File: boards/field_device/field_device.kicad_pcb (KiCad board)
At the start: 4 copper layers, 50 x 55 mm, 52 parts, among them SW1 TS-1088-AR02016, U1 CHT20MEMS, U2 STM32C051F8P6, U3 SPA06-003, U4 CN3163, U5 TPS63900, U6 SX1262IMLTRT, Y1 X322532MMB4SI

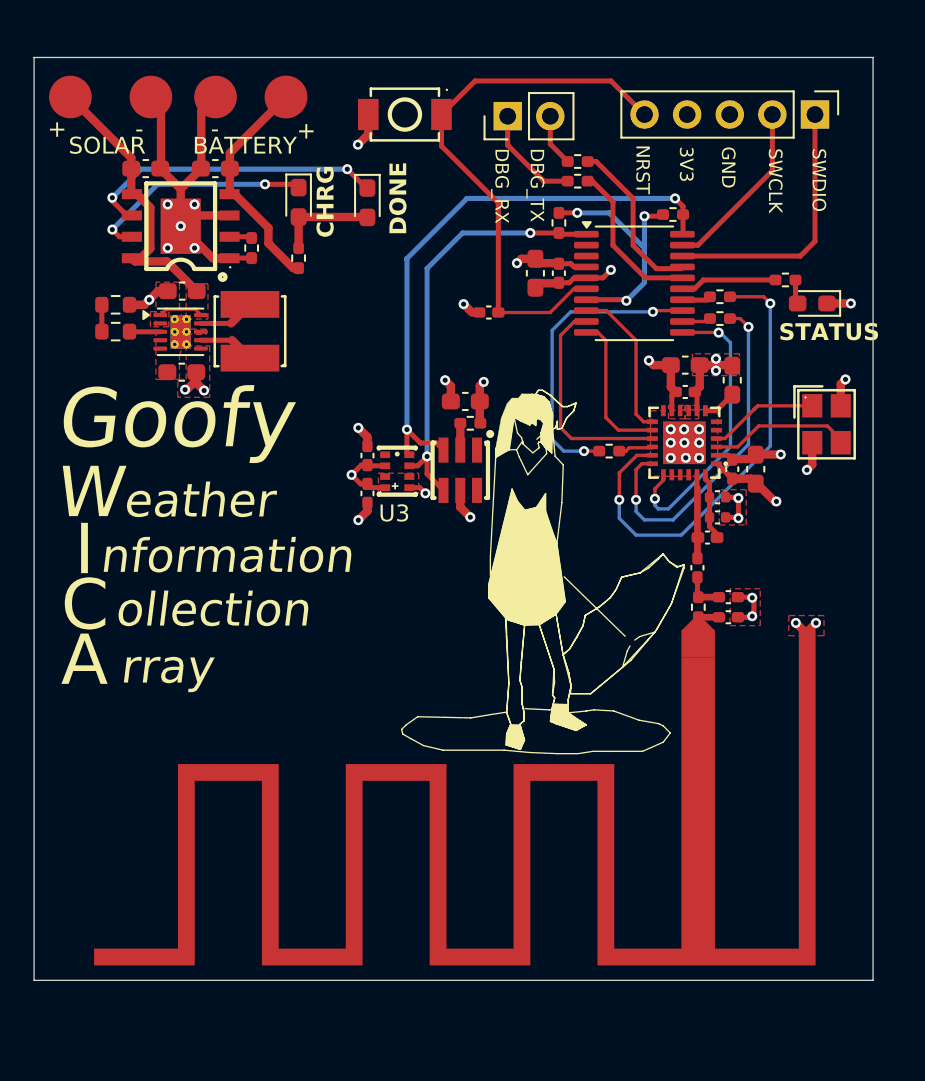
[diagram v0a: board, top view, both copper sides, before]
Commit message: change components to fit manufacturing capability
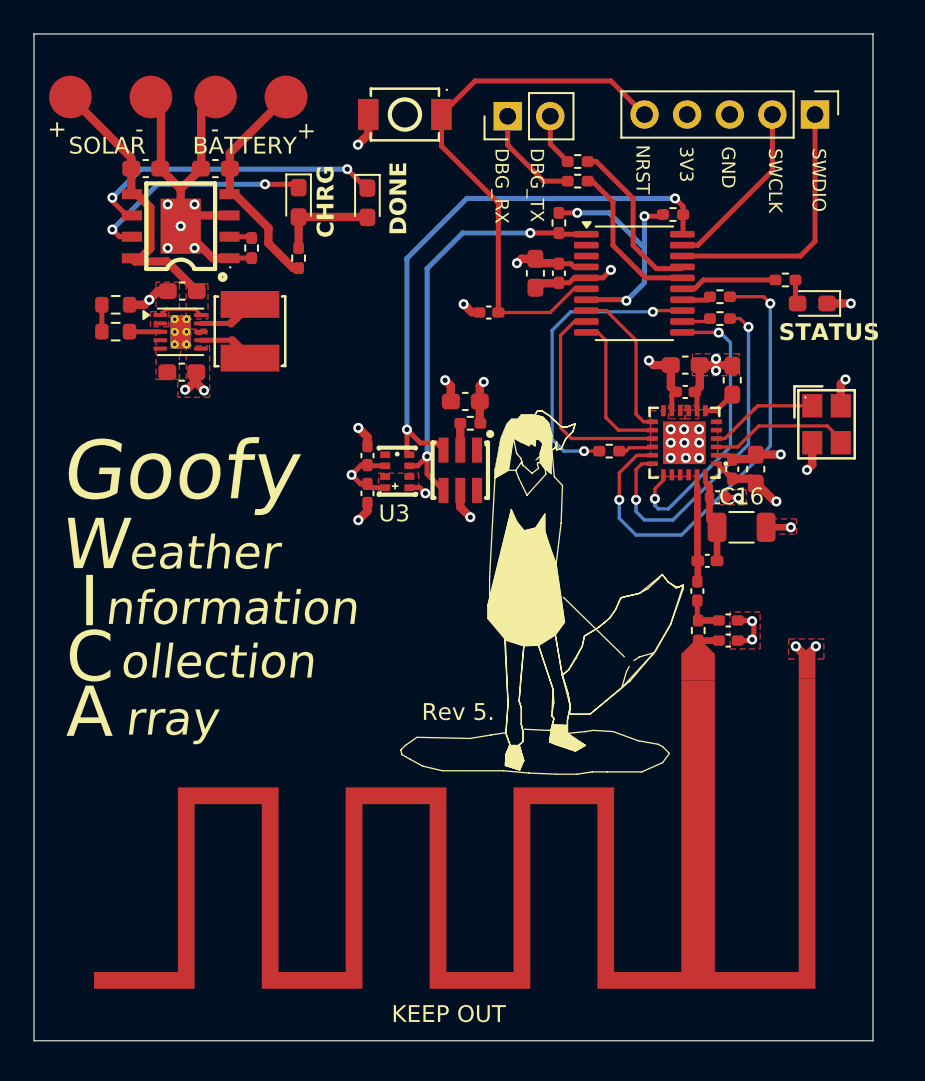
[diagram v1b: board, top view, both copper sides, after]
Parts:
- C1, C11, C12, C13: value 10u -> 10uF
- C14, C15, C2: value 100n -> 100nF
- C16: value 47n -> 47nF C0G; footprint Capacitor_SMD:C_0402_1005Metric -> Resistor_SMD:R_1206_3216Metric
- C17, C18: value 100p -> 100p C0G
- L2: value 47n -> 47nH
- moved C16 1.55 mm to (71.9, 51.4)
- moved AE1 1.39 mm to (76.3, 78.9)
- moved C18 1.39 mm to (69.2, 55.2)
- moved C19 1.39 mm to (71.1, 57.0)
- moved C20 1.39 mm to (71.1, 58.1)
- moved L2 1.39 mm to (69.8, 53.4)
- moved R15 1.39 mm to (69.3, 57.6)
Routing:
- net /lora_module/VR_PA: track 4.11 -> 6.20 mm
- net /lora_module/RFO: track 8.78 -> 10.0 mm
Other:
- board size 50 x 55 mm -> 50 x 60 mm
- board text added: "KEEP OUT"
- board text added: "Rev 5."

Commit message: idk atp
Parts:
- C1, C11, C12, C13, C3, C7, C8, C9: value 10uF -> CL10A106KP8NNNC 10uF
- C10: value 22uF -> CL10A226MQ8NRNC 22uF
- C14, C15, C2, C4, C5, C6: value 100nF -> CL05B104KO5NNNC 100nF
- C16: value 47nF C0G -> 47nF
- C17, C18: value 100p C0G -> 0402CG101J500NT 100pF
- L2: footprint Inductor_SMD:L_0402_1005Metric_Pad0.77x0.64mm_HandSolder -> Inductor_SMD:L_0805_2012Metric_Pad1.05x1.20mm_HandSolder
- R1: value 330R -> 0603WAF3300T5E 330R; footprint Resistor_SMD:R_0402_1005Metric_Pad0.72x0.64mm_HandSolder -> Capacitor_SMD:C_0603_1608Metric
- R10, R2, R3: value 10k -> 0402WGF1002TCE 10k
- R5, R6, R7: value 22R -> 0402WGF220JTCE 22R
- moved C1 0.67 mm to (55.9, 43.5)
- moved R15 0.40 mm to (69.2, 58.0)
- moved C18 0.40 mm to (69.2, 55.6)
- moved C19 0.40 mm to (71.1, 57.4)
- moved C20 0.40 mm to (71.1, 58.5)
- moved AE1 0.40 mm to (76.3, 79.3)
- moved L2 0.29 mm to (70.1, 53.5)
- moved R1 0.20 mm to (55.9, 45.2)

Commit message: peer review
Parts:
- C16: footprint Resistor_SMD:R_1206_3216Metric -> Capacitor_SMD:C_0603_1608Metric
- C17: value 0402CG101J500NT 100pF -> CL05B104KO5NNNC 100nF
- moved C18 1.10 mm to (69.2, 54.5)
- moved L2 1.04 mm to (70.4, 52.5)
- moved C19 0.95 mm to (71.1, 56.4)
- moved C20 0.95 mm to (71.1, 57.6)
- moved R15 0.95 mm to (69.2, 57.0)
- moved C16 0.83 mm to (71.2, 50.9)
- moved C17 0.47 mm to (70.9, 49.6)
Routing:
- net +3.3V: track 23.8 -> 18.5 mm
- net GND: track 62.8 -> 59.4 mm, vias 35 -> 34
- net /MCU/SWDIO: track 15.8 -> 14.3 mm
- net /lora_module/RFO: track 10.0 -> 11.0 mm
- net /lora_module/VR_PA: track 5.87 -> 5.17 mm
